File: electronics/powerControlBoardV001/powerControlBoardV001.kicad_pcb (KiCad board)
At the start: 2 copper layers, 100 x 100 mm, 75 parts, among them J1 Conn_01x03, J2 Conn_01x02, J3 Conn_01x02, K1 FINDER-40.52, Q1 Q_NMOS_GSD, Q2 MMBT3904, Q3 MMBT3904, Q4 MMBT3904, Q5 MMBT3904, Q6 MMBT3904, Q7 MMBT3904, U1 4N28, U2 4N28, U3 4N28

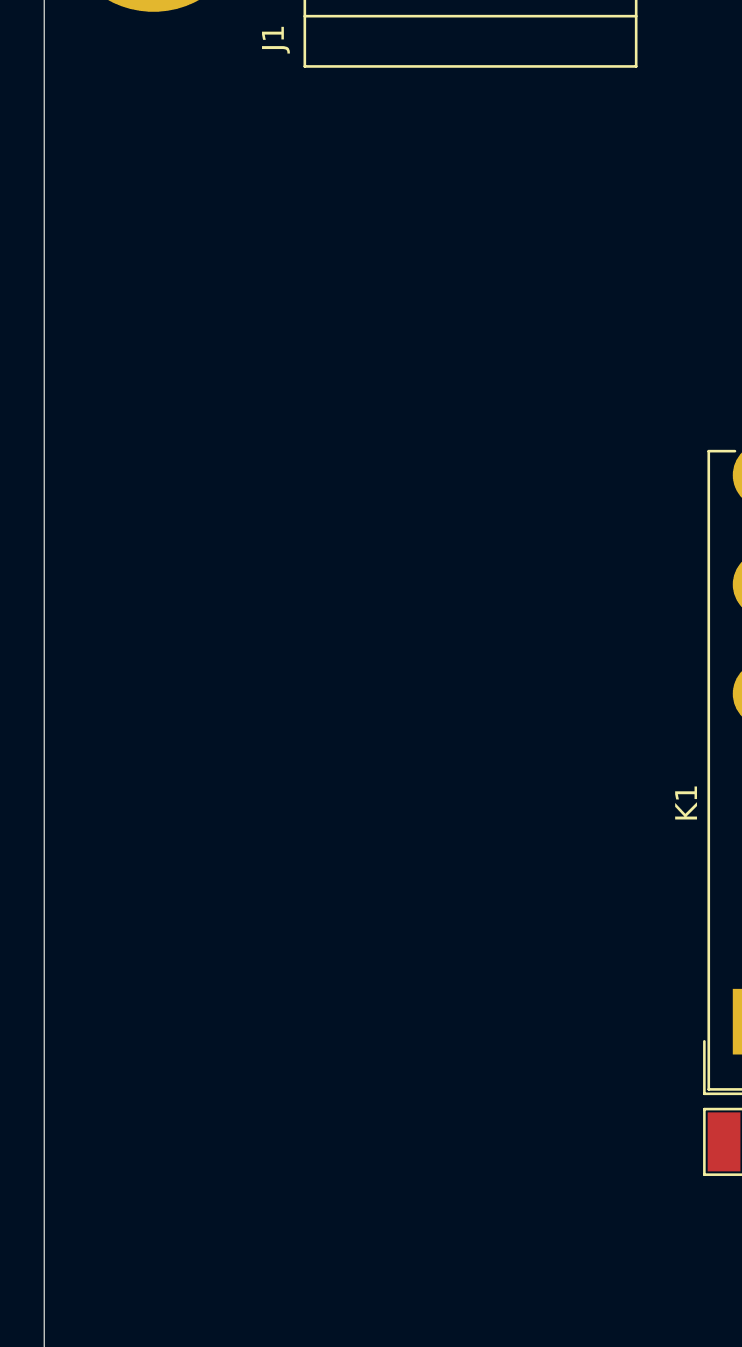
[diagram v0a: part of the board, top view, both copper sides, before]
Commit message: added hv psu section
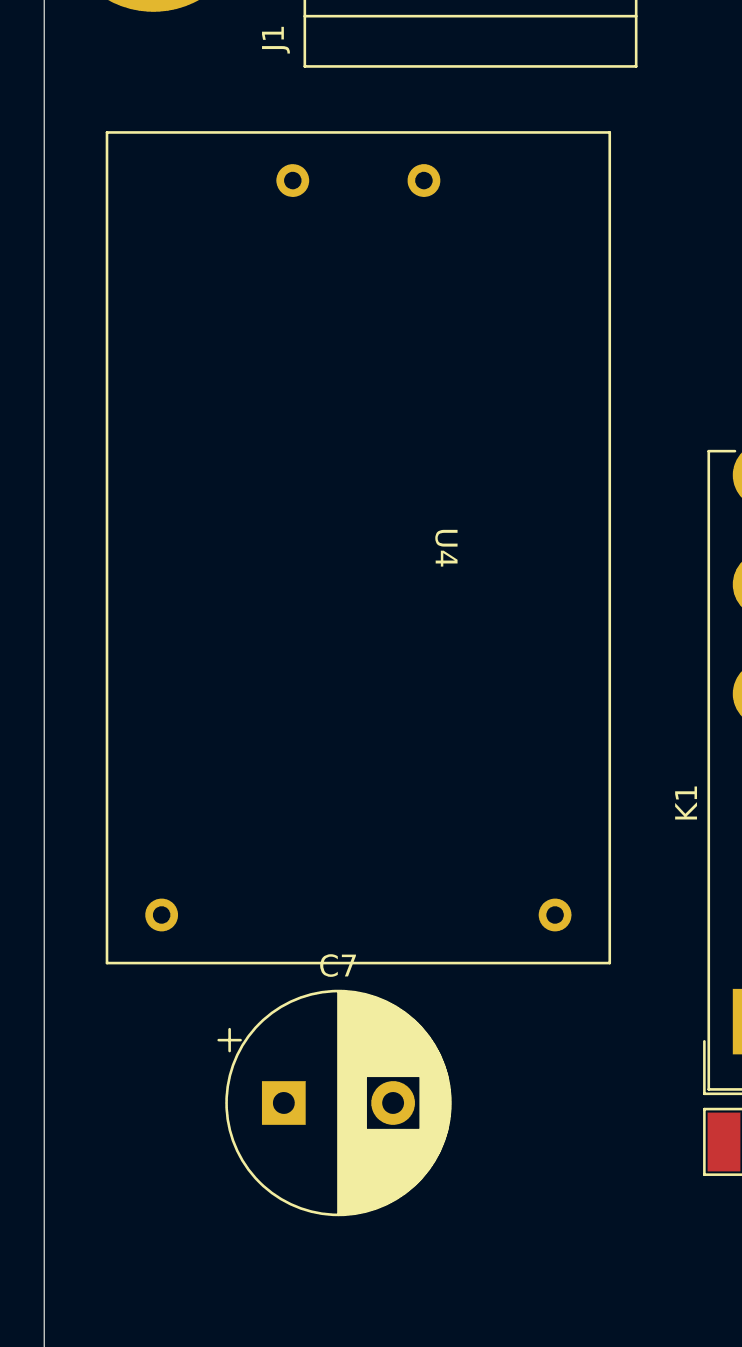
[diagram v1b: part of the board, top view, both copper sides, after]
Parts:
- added C7: 220u, Capacitor_THT:CP_Radial_D10.0mm_P5.00mm, F.Cu at (61.0, 109.2)
- added U4: HLK-5M12, SquantorHi-link:5MXX_series, F.Cu at (64.4, 83.8)
